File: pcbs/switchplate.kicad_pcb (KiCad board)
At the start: 2 copper layers, 155.6 x 164.6 mm, 0 parts

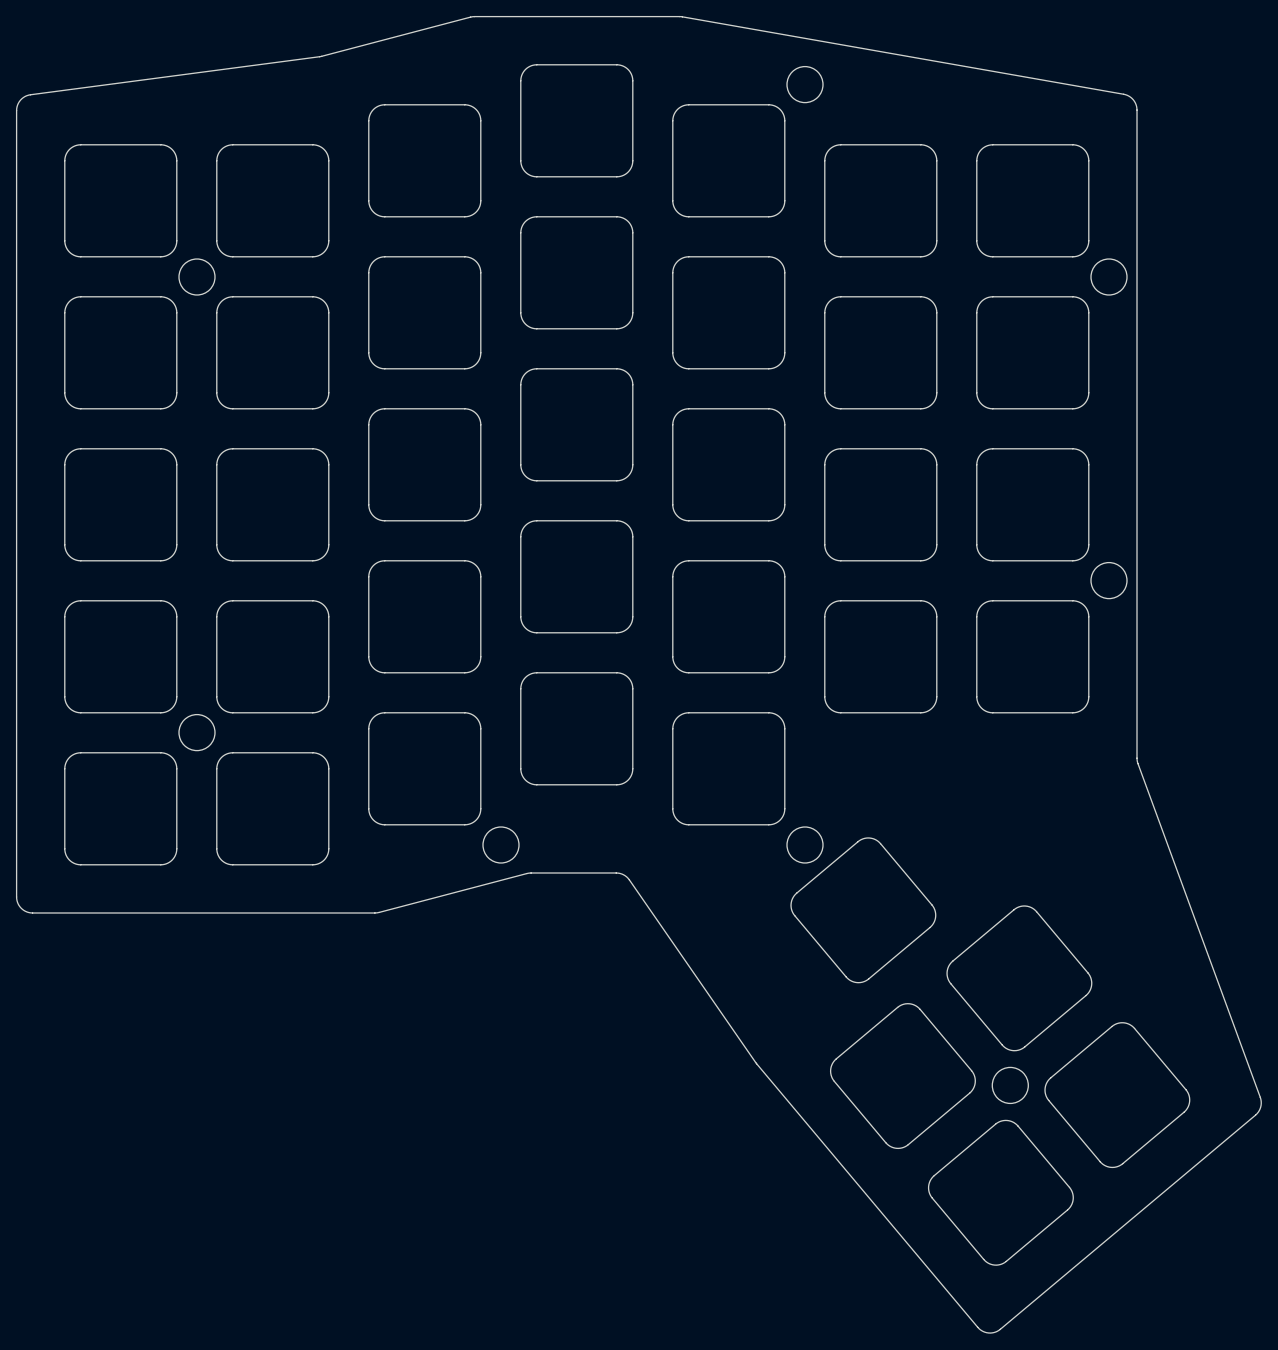
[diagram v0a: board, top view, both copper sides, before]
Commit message: Use a drill for all screw holes on generated pcb plates
don't plate the encoder mounting holes (kicad jlcpcb violation)
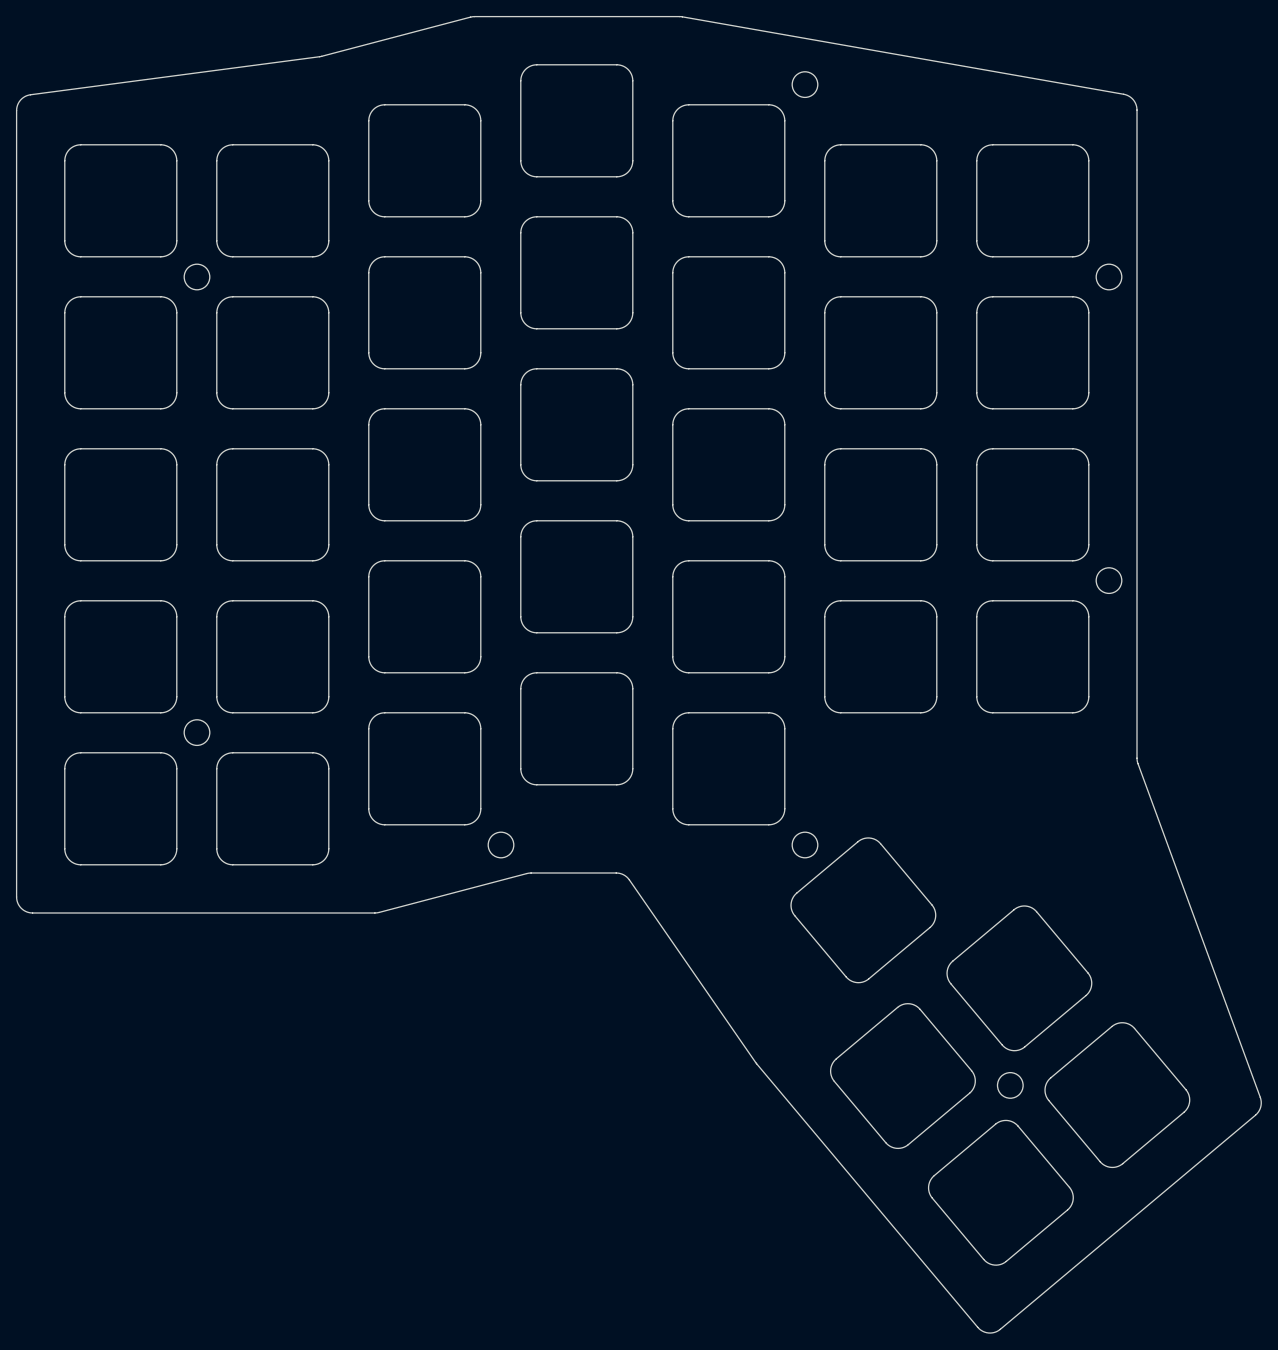
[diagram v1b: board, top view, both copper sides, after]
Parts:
- added MH1: , ceoloide:mounting_hole_npth, F.Cu at (59.5, 58.5)
- added MH2: , ceoloide:mounting_hole_npth, F.Cu at (135.5, 34.5)
- added MH3: , ceoloide:mounting_hole_npth, F.Cu at (173.5, 58.5)
- added MH4: , ceoloide:mounting_hole_npth, F.Cu at (59.5, 115.5)
- added MH5: , ceoloide:mounting_hole_npth, F.Cu at (135.5, 129.5)
- added MH6: , ceoloide:mounting_hole_npth, F.Cu at (97.5, 129.5)
- added MH7: , ceoloide:mounting_hole_npth, F.Cu at (161.2, 159.6)
- added MH8: , ceoloide:mounting_hole_npth, F.Cu at (173.5, 96.5)
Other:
- outline, holes or cut-outs redrawn
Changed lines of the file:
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@@
   (title_block
     (title "switchplate")
-    (date "2026-10-29")
+    (date "2026-10-30")
     (rev "0.1")
     (company "aevumdecessus")
@@
   )
   (net 0 "")
+  (footprint "ceoloide:mounting_hole_npth"
+    (layer "F.Cu")
+    (at 59.525 58.525 0)
+    (property "Reference" "MH1"
+      (at 0 2.55 0)
+      (layer "F.SilkS")
+      hide
+      (effects (font (size 1 1) (thickness 0.15)))
+    )
+    (pad "" np_thru_hole circle
+      (at 0 0 0)
+      (size 3.2 3.2)
+      (drill 3.2)
+      (layers "*.Cu" "*.Mask")
+    )
+  )
+  (footprint "ceoloide:mounting_hole_npth"
+    (layer "F.Cu")
+    (at 135.525 34.475 0)
+    (property "Reference" "MH2"
+      (at 0 2.55 0)
+      (layer "F.SilkS")
+      hide
+      (effects (font (size 1 1) (thickness 0.15)))
+    )
+    (pad "" np_thru_hole circle
+      (at 0 0 0)
+      (size 3.2 3.2)
+      (drill 3.2)
+      (layers "*.Cu" "*.Mask")
+    )
+  )
+  (footprint "ceoloide:mounting_hole_npth"
+    (layer "F.Cu")
+    (at 173.525 58.525 0)
+    (property "Reference" "MH3"
+      (at 0 2.55 0)
+      (layer "F.SilkS")
+      hide
+      (effects (font (size 1 1) (thickness 0.15)))
+    )
+    (pad "" np_thru_hole circle
+      (at 0 0 0)
+      (size 3.2 3.2)
+      (drill 3.2)
+      (layers "*.Cu" "*.Mask")
+    )
+  )
+  (footprint "ceoloide:mounting_hole_npth"
+    (layer "F.Cu")
+    (at 59.525 115.475 0)
+    (property "Reference" "MH4"
+      (at 0 2.55 0)
+      (layer "F.SilkS")
+      hide
+      (effects (font (size 1 1) (thickness 0.15)))
+    )
+    (pad "" np_thru_hole circle
+      (at 0 0 0)
+      (size 3.2 3.2)
+      (drill 3.2)
+      (layers "*.Cu" "*.Mask")
+    )
+  )
+  (footprint "ceoloide:mounting_hole_npth"
+    (layer "F.Cu")
+    (at 135.525 129.525 0)
+    (property "Reference" "MH5"
+      (at 0 2.55 0)
+      (layer "F.SilkS")
+      hide
+      (effects (font (size 1 1) (thickness 0.15)))
+    )
+    (pad "" np_thru_hole circle
+      (at 0 0 0)
+      (size 3.2 3.2)
+      (drill 3.2)
+      (layers "*.Cu" "*.Mask")
+    )
+  )
+  (footprint "ceoloide:mounting_hole_npth"
+    (layer "F.Cu")
+    (at 97.525 129.525 0)
+    (property "Reference" "MH6"
+      (at 0 2.55 0)
+      (layer "F.SilkS")
+      hide
+      (effects (font (size 1 1) (thickness 0.15)))
+    )
+    (pad "" np_thru_hole circle
+      (at 0 0 0)
+      (size 3.2 3.2)
+      (drill 3.2)
+      (layers "*.Cu" "*.Mask")
+    )
+  )
+  (footprint "ceoloide:mounting_hole_npth"
+    (layer "F.Cu")
+    (at 161.1892292 159.579668 -50)
+    (property "Reference" "MH7"
+      (at 0 2.55 -50)
+      (layer "F.SilkS")
+      hide
+      (effects (font (size 1 1) (thickness 0.15)))
+    )
+    (pad "" np_thru_hole circle
+      (at 0 0 -50)
+      (size 3.2 3.2)
+      (drill 3.2)
+      (layers "*.Cu" "*.Mask")
+    )
+  )
+  (footprint "ceoloide:mounting_hole_npth"
+    (layer "F.Cu")
+    (at 173.525 96.475 0)
+    (property "Reference" "MH8"
+      (at 0 2.55 0)
+      (layer "F.SilkS")
+      hide
+      (effects (font (size 1 1) (thickness 0.15)))
+    )
+    (pad "" np_thru_hole circle
+      (at 0 0 0)
+      (size 3.2 3.2)
+      (drill 3.2)
+      (layers "*.Cu" "*.Mask")
+    )
+  )
   (gr_line (start 36.975 136.025) (end 36.975 37.72908083684211) (layer Edge.Cuts) (stroke (width 0.15) (type default)))
 (gr_line (start 38.714091 35.746172236842106) (end 74.84941700000002 30.991524078947368) (layer Edge.Cuts) (stroke (width 0.15) (type default)))
@@
 (gr_arc (start 81.76624681999995 138.025) (mid 82.02286121999995 138.0084689) (end 82.27523341999995 137.95914910000002) (layer Edge.Cuts) (stroke (width 0.15) (type default)))
 (gr_arc (start 36.975 136.025) (mid 37.5607864 137.43921360000002) (end 38.975 138.025) (layer Edge.Cuts) (stroke (width 0.15) (type default)))
-(gr_circle (center 59.525 58.525) (end 61.775 58.525) (layer Edge.Cuts) (stroke (width 0.15) (type default)) (fill none))
-(gr_circle (center 135.525 34.475) (end 137.775 34.475) (layer Edge.Cuts) (stroke (width 0.15) (type default)) (fill none))
-(gr_circle (center 173.525 58.525) (end 175.775 58.525) (layer Edge.Cuts) (stroke (width 0.15) (type default)) (fill none))
-(gr_circle (center 59.525 115.475) (end 61.775 115.475) (layer Edge.Cuts) (stroke (width 0.15) (type default)) (fill none))
-(gr_circle (center 135.525 129.525) (end 137.775 129.525) (layer Edge.Cuts) (stroke (width 0.15) (type default)) (fill none))
-(gr_circle (center 97.525 129.525) (end 99.775 129.525) (layer Edge.Cuts) (stroke (width 0.15) (type default)) (fill none))
-(gr_circle (center 161.1892292 159.579668) (end 163.4392292 159.579668) (layer Edge.Cuts) (stroke (width 0.15) (type default)) (fill none))
-(gr_circle (center 173.525 96.475) (end 175.775 96.475) (layer Edge.Cuts) (stroke (width 0.15) (type default)) (fill none))
 (gr_line (start 45 132) (end 55 132) (layer Edge.Cuts) (stroke (width 0.15) (type default)))
 (gr_line (start 57 130) (end 57 120) (layer Edge.Cuts) (stroke (width 0.15) (type default)))
